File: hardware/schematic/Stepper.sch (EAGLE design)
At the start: 20 parts

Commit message: schematic updates
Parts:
- removed SV1, SV2: (no value), con-lstb:MA04-1
- removed U$1: NEMA23, Motors:NEMA23
- added CUSB6: 10uF, rcl:C-EUC0805
- added D17: 1N5819HW-7-F, 1N5819HW-7-F:1N5819HW-7-F
- added D18, D19, D20: CPDQ5V0-HF, CPDQ5V0-HF:CPDQ5V0-HF
- added LED5: (no value), adafruit:LED
- added RLEDOUT10: 2.2k, rcl:R-US_M0805
- added RLEDOUT4, RLEDOUT5: 10k, rcl:R-US_M0805
- added RUSB8, RUSB9: 5.1k, rcl:R-US_M0805
- added STEPPER_PINOUT1: (no value), con-lstb:MA04-1
- added STEPPER_PINOUT2: (no value), con-lstb:MA05-1
- added STEPPER_REGULATOR: AZ1117IH-3.3TRG1, AZ1117IH-3.3TRG1:AZ1117IH-3.3TRG1
- added STEPPER_USBC_OUT: USB4110-GF-A, USB4110-GF-A:USB4110-GF-A
- added U$8, U$9: NC_MARKER, NC_MARKER:NC_MARKER
- added U16: MMSZ5225BT1G, MMSZ5225BT1G:MMSZ5225BT1G
- added U19: LM358DR, LM358DR:LM358DR
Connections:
- removed net 0: CVINT.2, CVMOT.1, CVMOT2.1, CVMOT3.1, CVMOT4.1, R1.A, RADECAY.2, RAISEN.2, RBDECAY.2, RBISEN.2, STEPPER_CONTROLLER.EXP(GND), STEPPER_CONTROLLER.GND
- removed net 3.3VOUT: CVINT.1, RFAULT.2, RFAULT1.1, STEPPER_CONTROLLER.VINT
- removed net 5VOUT: CVCP.1, CVMOT.2, CVMOT2.2, CVMOT3.2, RVMOT.2, STEPPER_CONTROLLER.VM
- removed net AOUT1: U$1.BLK-A
- removed net AOUT2: U$1.GRN-C
- removed net BOUT1: U$1.RED-B
- removed net BOUT2: U$1.BLU-D
- removed net GPIO8: STEPPER_CONTROLLER.STEP/BENBL
- removed net GPIO9: STEPPER_CONTROLLER.DIR/BPHASE
- new net 3.3VOUTUSB2: CVINT.1, LED5.A, RFAULT.2, RFAULT1.1, RLEDOUT4.2, RLEDOUT5.2, STEPPER_CONTROLLER.VINT, STEPPER_REGULATOR.OUTPUT
- new net 5VOUTUSB22: CUSB6.1, CVCP.1, CVMOT.2, CVMOT2.2, CVMOT3.2, D17.K, RVMOT.2, STEPPER_CONTROLLER.VM, STEPPER_REGULATOR.INPUT, U19.VCC
- new net GND: CUSB6.2, CVINT.2, CVMOT.1, CVMOT2.1, CVMOT3.1, CVMOT4.1, D18.K, D19.K, D20.K, R1.A, RADECAY.2, RAISEN.2, RBDECAY.2, RBISEN.2, RUSB8.2, RUSB9.2, STEPPER_CONTROLLER.EXP(GND), STEPPER_CONTROLLER.GND, STEPPER_REGULATOR.GND, STEPPER_USBC_OUT.GND, STEPPER_USBC_OUT.GND_2, U16.ANODE, U19.GND
- new net GPIO8M: D19.A, STEPPER_CONTROLLER.STEP/BENBL, STEPPER_USBC_OUT.DP1, STEPPER_USBC_OUT.DP2
- new net GPIO9M: D20.A, STEPPER_CONTROLLER.DIR/BPHASE, STEPPER_USBC_OUT.DN1, STEPPER_USBC_OUT.DN2
- new net N$72: RUSB8.1, STEPPER_USBC_OUT.CC1
- new net N$73: RUSB9.1, STEPPER_USBC_OUT.CC2
- new net N$82: RLEDOUT4.1, U16.CATHODE, U19.1IN+
- new net N$83: RLEDOUT5.1, U19.1IN-
- new net N$84: RLEDOUT10.2, U19.1OUT
- new net N$87: U$9.P$1, U19.2IN-
- new net N$88: LED5.C, RLEDOUT10.1
- new net N$89: U$8.P$1, U19.2IN+
- new net N$90: STEPPER_CONTROLLER.NENBL/AENBL, STEPPER_PINOUT2.5
- new net VBUS22: D17.A, D18.A, STEPPER_USBC_OUT.VBUS, STEPPER_USBC_OUT.VBUS_2
- net N$28: now also STEPPER_PINOUT1.1; no longer SV1.1
- net N$29: now also STEPPER_PINOUT1.2; no longer SV1.2
- net N$30: now also STEPPER_PINOUT1.3; no longer SV1.3
- net N$31: now also STEPPER_PINOUT1.4; no longer SV1.4
- net N$34: now also STEPPER_PINOUT2.4; no longer SV2.4
- net N$35: now also STEPPER_PINOUT2.3; no longer SV2.3
- net N$37: now also STEPPER_PINOUT2.1; no longer SV2.1
- net N$38: now also STEPPER_PINOUT2.2; no longer SV2.2
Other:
- note added: "Stepper Motor Control"
- moved on the sheet: CVCP, CVINT, CVMOT, CVMOT2, CVMOT3, CVMOT4, R1, RADECAY, RAISEN, RBDECAY, RBISEN, RFAULT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

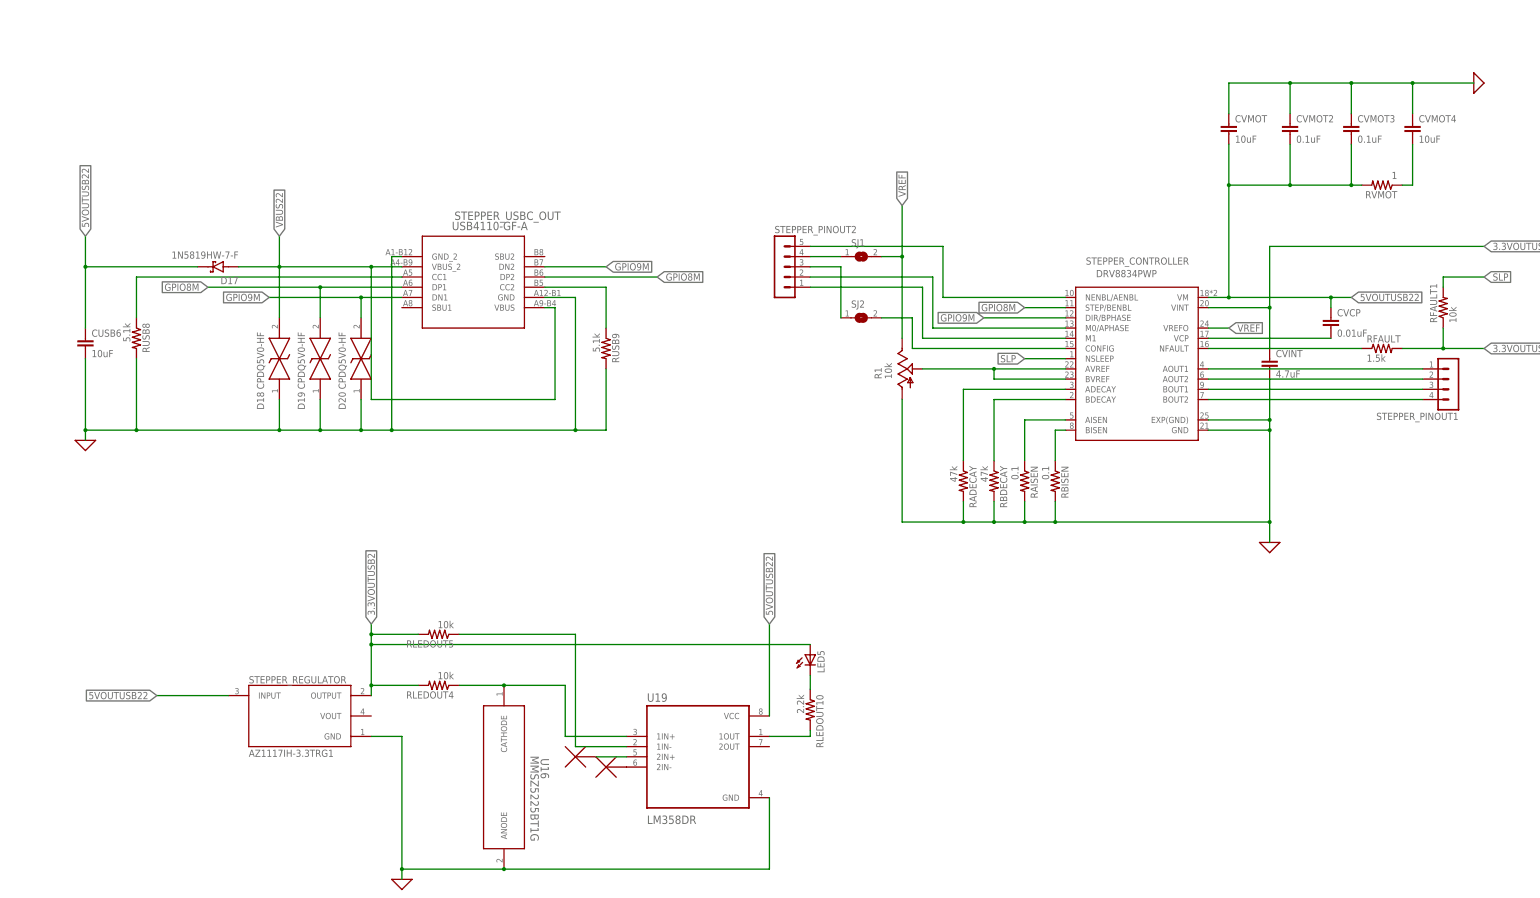
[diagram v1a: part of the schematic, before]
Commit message: Added regulators and SD Card. Needs major work
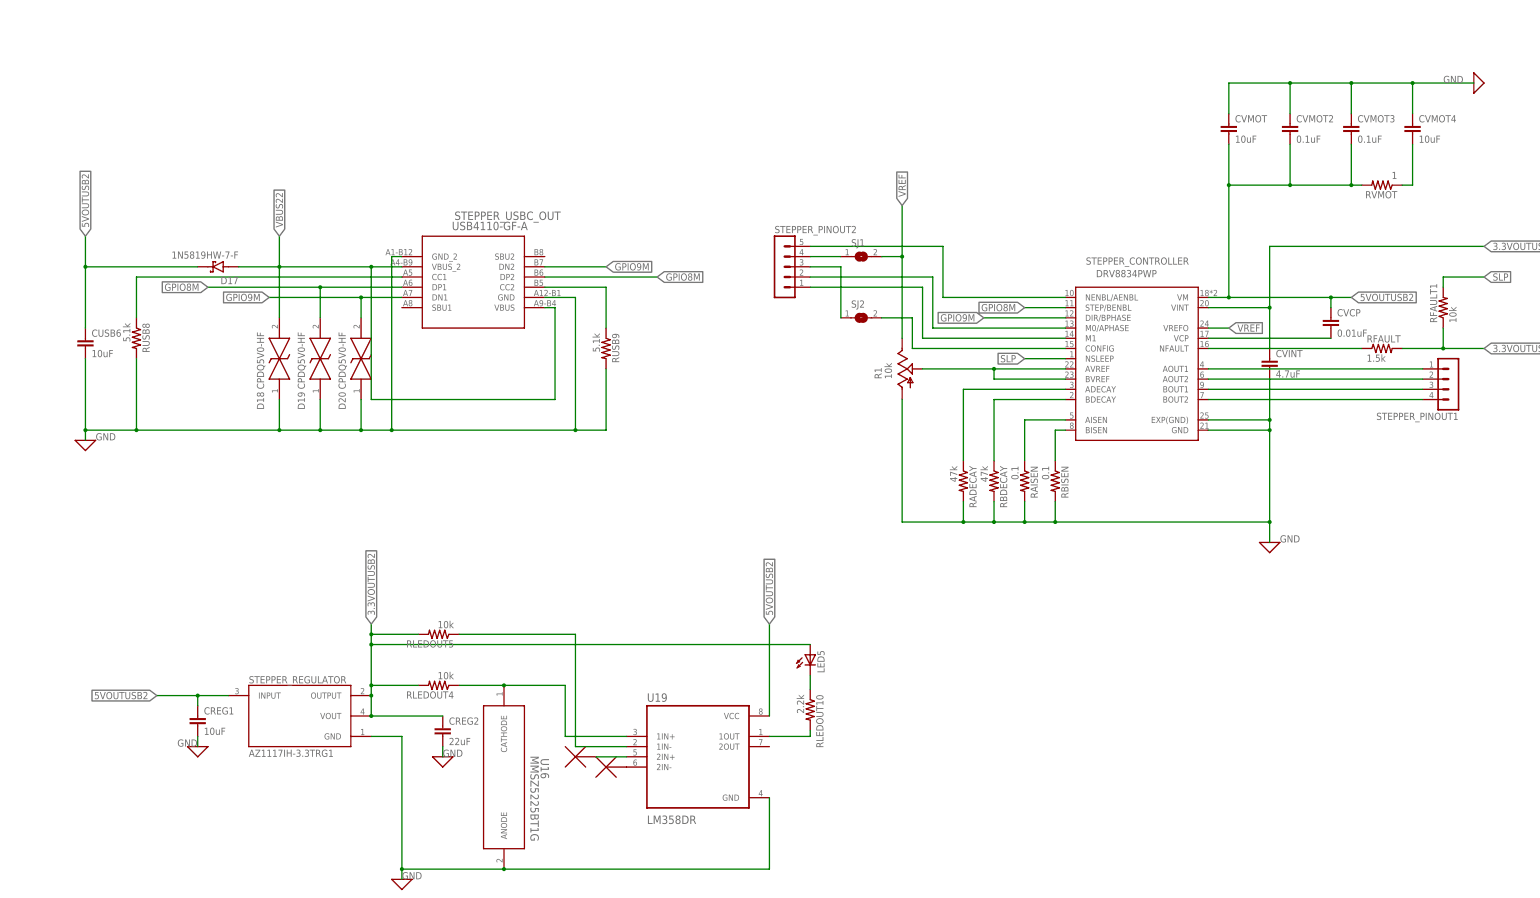
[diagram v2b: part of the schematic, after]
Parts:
- added CREG1: 10uF, rcl:C-EUC0805
- added CREG2: 22uF, rcl:C-EUC0805
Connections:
- removed net 5VOUTUSB22: CUSB6.1, CVCP.1, CVMOT.2, CVMOT2.2, CVMOT3.2, D17.K, RVMOT.2, STEPPER_CONTROLLER.VM, STEPPER_REGULATOR.INPUT, U19.VCC
- new net 5VOUTUSB2: CREG1.1, CUSB6.1, CVCP.1, CVMOT.2, CVMOT2.2, CVMOT3.2, D17.K, RVMOT.2, STEPPER_CONTROLLER.VM, STEPPER_REGULATOR.INPUT, U19.VCC
- net 3.3VOUTUSB2: now also CREG2.1, STEPPER_REGULATOR.VOUT
- net GND: now also CREG1.2, CREG2.2
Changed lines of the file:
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@@
 <part name="U$9" library="NC_MARKER" deviceset="NC_MARKER" device=""/>
 <part name="STEPPER_PINOUT2" library="con-lstb" library_urn="urn:adsk.eagle:library:162" deviceset="MA05-1" device="" package3d_urn="urn:adsk.eagle:package:8332/1"/>
+<part name="CREG1" library="rcl" library_urn="urn:adsk.eagle:library:334" deviceset="C-EU" device="C0805" package3d_urn="urn:adsk.eagle:package:23617/2" value="10uF"/>
+<part name="X_1" library="ngspice-simulation" library_urn="urn:adsk.eagle:library:527439" deviceset="GND" device=""/>
+<part name="X_2" library="ngspice-simulation" library_urn="urn:adsk.eagle:library:527439" deviceset="GND" device=""/>
+<part name="CREG2" library="rcl" library_urn="urn:adsk.eagle:library:334" deviceset="C-EU" device="C0805" package3d_urn="urn:adsk.eagle:package:23617/2" value="22uF"/>
 </parts>
 <sheets>
@@
 <attribute name="VALUE" x="-46.99" y="50.8" size="1.778" layer="96"/>
 <attribute name="NAME" x="-46.99" y="69.342" size="1.778" layer="95"/>
+</instance>
+<instance part="CREG1" gate="G$1" x="-190.5" y="-50.8" smashed="yes">
+<attribute name="NAME" x="-188.976" y="-50.419" size="1.778" layer="95"/>
+<attribute name="VALUE" x="-188.976" y="-55.499" size="1.778" layer="96"/>
+</instance>
+<instance part="X_1" gate="G$1" x="-190.5" y="-58.42" smashed="yes"/>
+<instance part="X_2" gate="G$1" x="-129.54" y="-60.96" smashed="yes"/>
+<instance part="CREG2" gate="G$1" x="-129.54" y="-53.34" smashed="yes">
+<attribute name="NAME" x="-128.016" y="-52.959" size="1.778" layer="95"/>
+<attribute name="VALUE" x="-128.016" y="-58.039" size="1.778" layer="96"/>
 </instance>
 </instances>
@@
 </segment>
 </net>
-<net name="5VOUTUSB22" class="0">
+<net name="5VOUTUSB2" class="0">
 <segment>
 <pinref part="D17" gate="G$1" pin="K"/>
@@
 <segment>
 <pinref part="STEPPER_REGULATOR" gate="G$1" pin="INPUT"/>
-<wire x1="-182.88" y1="-45.72" x2="-200.66" y2="-45.72" width="0.1524" layer="91"/>
+<wire x1="-182.88" y1="-45.72" x2="-190.5" y2="-45.72" width="0.1524" layer="91"/>
 <label x="-200.66" y="-45.72" size="1.778" layer="95" rot="R180" xref="yes"/>
+<pinref part="CREG1" gate="G$1" pin="1"/>
+<wire x1="-190.5" y1="-45.72" x2="-200.66" y2="-45.72" width="0.1524" layer="91"/>
+<wire x1="-190.5" y1="-48.26" x2="-190.5" y2="-45.72" width="0.1524" layer="91"/>
+<junction x="-190.5" y="-45.72"/>
 </segment>
 <segment>
@@
 <junction x="-147.32" y="-33.02"/>
 <pinref part="LED5" gate="G$1" pin="A"/>
+<pinref part="STEPPER_REGULATOR" gate="G$1" pin="VOUT"/>
+<wire x1="-147.32" y1="-50.8" x2="-147.32" y2="-45.72" width="0.1524" layer="91"/>
+<junction x="-147.32" y="-45.72"/>
+<pinref part="CREG2" gate="G$1" pin="1"/>
+<wire x1="-129.54" y1="-50.8" x2="-147.32" y2="-50.8" width="0.1524" layer="91"/>
+<junction x="-147.32" y="-50.8"/>
 </segment>
 </net>
@@
 <wire x1="-15.24" y1="-2.54" x2="0" y2="-2.54" width="0.1524" layer="91"/>
 <junction x="0" y="-2.54"/>
+<label x="78.74" y="-7.62" size="1.778" layer="95"/>
 </segment>
 <segment>
@@
 <pinref part="CVMOT" gate="G$1" pin="1"/>
 <wire x1="66.04" y1="106.68" x2="66.04" y2="99.06" width="0.1524" layer="91"/>
+<label x="119.38" y="106.68" size="1.778" layer="95"/>
 </segment>
 <segment>
@@
 <wire x1="-149.86" y1="27.94" x2="-149.86" y2="20.32" width="0.1524" layer="91"/>
 <junction x="-149.86" y="20.32"/>
+<label x="-215.9" y="17.78" size="1.778" layer="95"/>
 </segment>
 <segment>
@@
 <wire x1="-48.26" y1="-88.9" x2="-48.26" y2="-71.12" width="0.1524" layer="91"/>
 <junction x="-114.3" y="-88.9"/>
+<label x="-139.7" y="-91.44" size="1.778" layer="95"/>
+</segment>
+<segment>
+<pinref part="X_1" gate="G$1" pin="0"/>
+<pinref part="CREG1" gate="G$1" pin="2"/>
+<wire x1="-190.5" y1="-58.42" x2="-190.5" y2="-55.88" width="0.1524" layer="91"/>
+<label x="-195.58" y="-58.42" size="1.778" layer="95"/>
+</segment>
+<segment>
+<pinref part="X_2" gate="G$1" pin="0"/>
+<pinref part="CREG2" gate="G$1" pin="2"/>
+<wire x1="-129.54" y1="-60.96" x2="-129.54" y2="-58.42" width="0.1524" layer="91"/>
+<label x="-129.54" y="-60.96" size="1.778" layer="95"/>
 </segment>
 </net>
@@
 </sheet>
 </sheets>
+<errors>
+</errors>
 </schematic>
 </drawing>
